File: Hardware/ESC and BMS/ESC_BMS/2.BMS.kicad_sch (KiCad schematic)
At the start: 36 parts, among them Q301 SQJ141ELP, Q302 NTD25P03LT4G, Q303 SQJ141ELP, Q304 NMOS, Q305 SQJ141ELP, SW301 SW_SPST, U301 BQ2057W, U302 BQ2969T

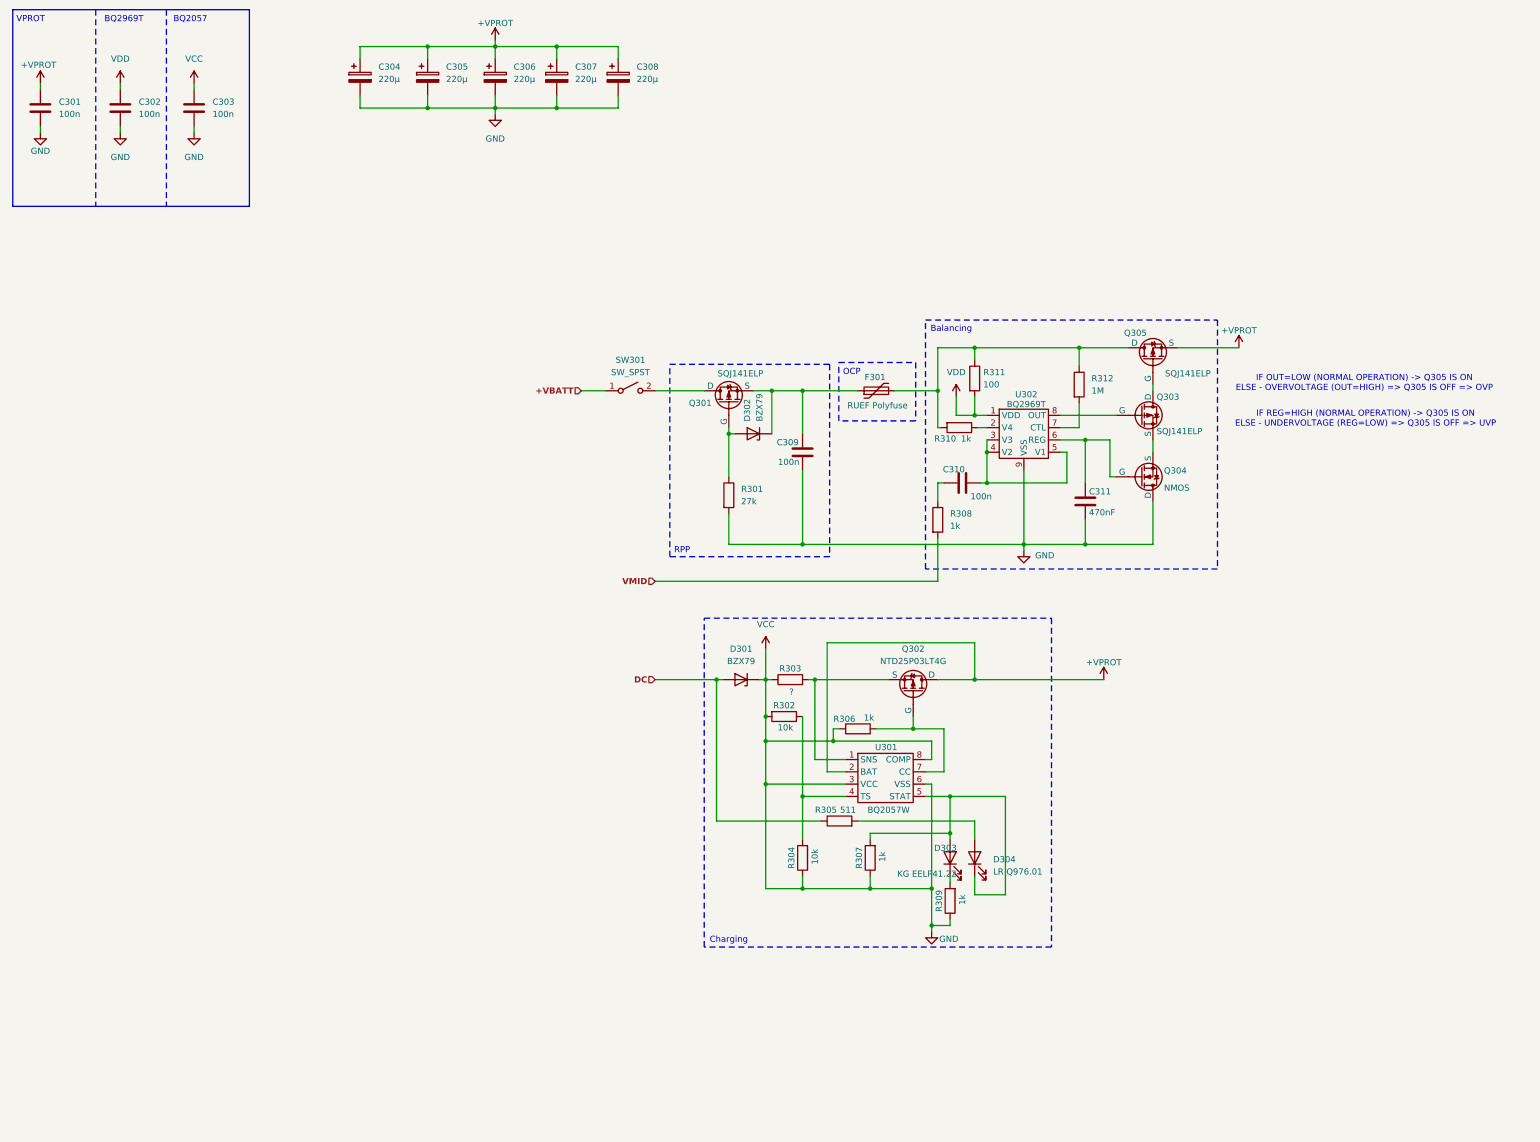
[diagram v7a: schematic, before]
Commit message: More BMS
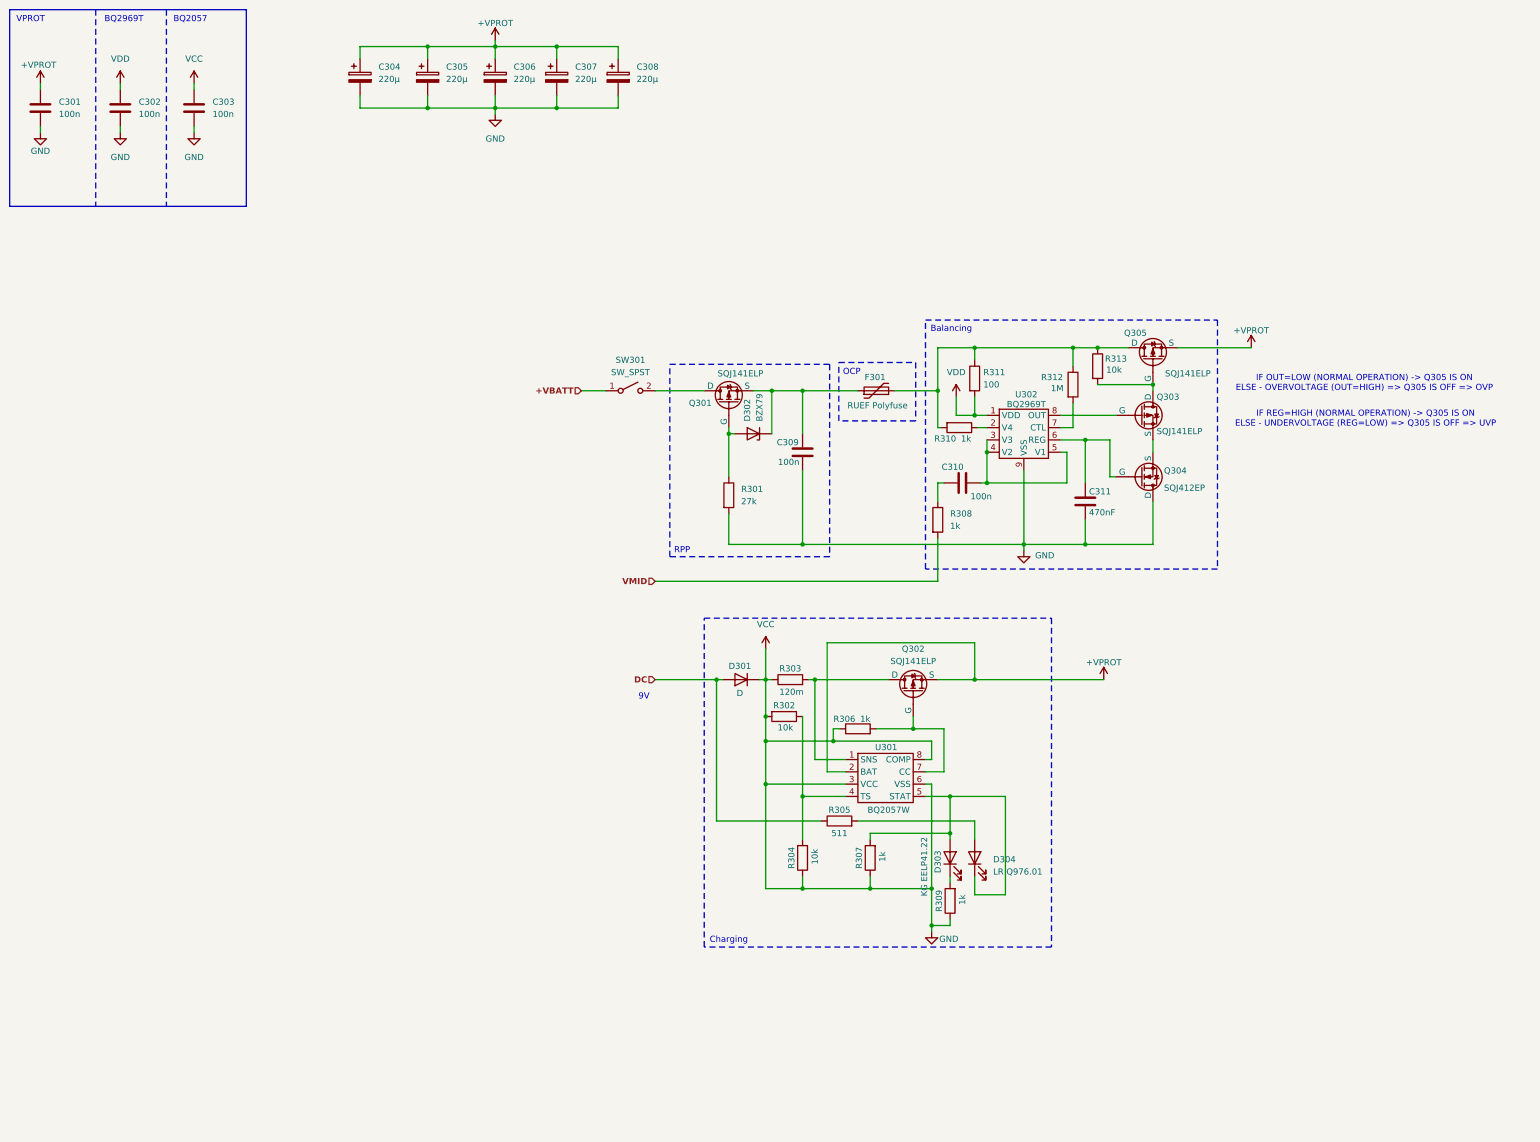
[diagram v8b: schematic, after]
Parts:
- removed D301: BZX79, Diode_THT:D_DO-35_SOD27_P10.16mm_Horizontal, symbol Diode:ZPDxx
- added D301: D, Diode_SMD:Vishay_SMPA, symbol Device:D
- added R313: 10k, Resistor_SMD:R_0603_1608Metric, symbol Device:R
- C311: footprint (none) -> Capacitor_SMD:C_1206_3216Metric_Pad1.33x1.80mm_HandSolder
- D303: footprint (none) -> https://docs.rs-online.com/e1fe/A700000013302439.pdf
- D304: footprint (none) -> https://docs.rs-online.com/01aa/A700000010723894.pdf
- Q301, Q303, Q305: footprint (none) -> Package_SO:PowerPAK_SO-8L_Single
- Q302: value NTD25P03LT4G -> SQJ141ELP; footprint (none) -> Package_SO:PowerPAK_SO-8L_Single
- Q304: value NMOS -> SQJ412EP; footprint (none) -> Package_SO:PowerPAK_SO-8L_Single
- R301, R302, R304: footprint (none) -> Resistor_SMD:R_0603_1608Metric
- R303: value ? -> 120m; footprint (none) -> Resistor_SMD:R_0805_2012Metric_Pad1.20x1.40mm_HandSolder
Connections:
- net +VPROT: now also Q302.3 (S); no longer Q302.1 (D)
- net DC: now also D301.2 (A)
- net GND: now also D301.1 (K)
- net at F301.2, Q305.1 (D), R310.2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: now also R313.1
- net at Q303.1 (D), Q305.2 (G): now also R313.2
- net at R303.2, U301.1 (SNS): now also Q302.1 (D); no longer Q302.3 (S)
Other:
- note added: "9V"
- moved on the sheet: Q302, R312
